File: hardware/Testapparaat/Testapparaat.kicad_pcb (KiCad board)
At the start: 2 copper layers, 138.9 x 89.6 mm, 107 parts, among them J1 IO_SD, J10 B-, J11 Display_shield, J12 GPIO_INPUTS, J13 FrontPanel, J14 GPIO_OUTPUT, J2 Module_1, J3 Module_2, J4 DEBUG, J5 FPC_40P_LCD_ILI9488, J6 IO_UART, J7 Emergency Stop Button, J8 CON-SOCJ-2155, J9 B+, Q1 BC817, Q2 BC817, Q3 BC817, Q4 IRFR9024N, Q5 IRFR9024N, Q6 IRFR9024N, SW1 RST, SW2 on/off switch, U1 74HC595 (SIPO Shift register), U10 LM2596S-5, U11 LM2596S-3.3, U12 74AUC1G74, U2 ESP32-WROOM-32, U4 74HC595 (SIPO Shift register), U5 TCA9534 (IO Expander), U6 74HC14, U7 TCA9534 (IO Expander), U8 74HC14, U9 74HC14

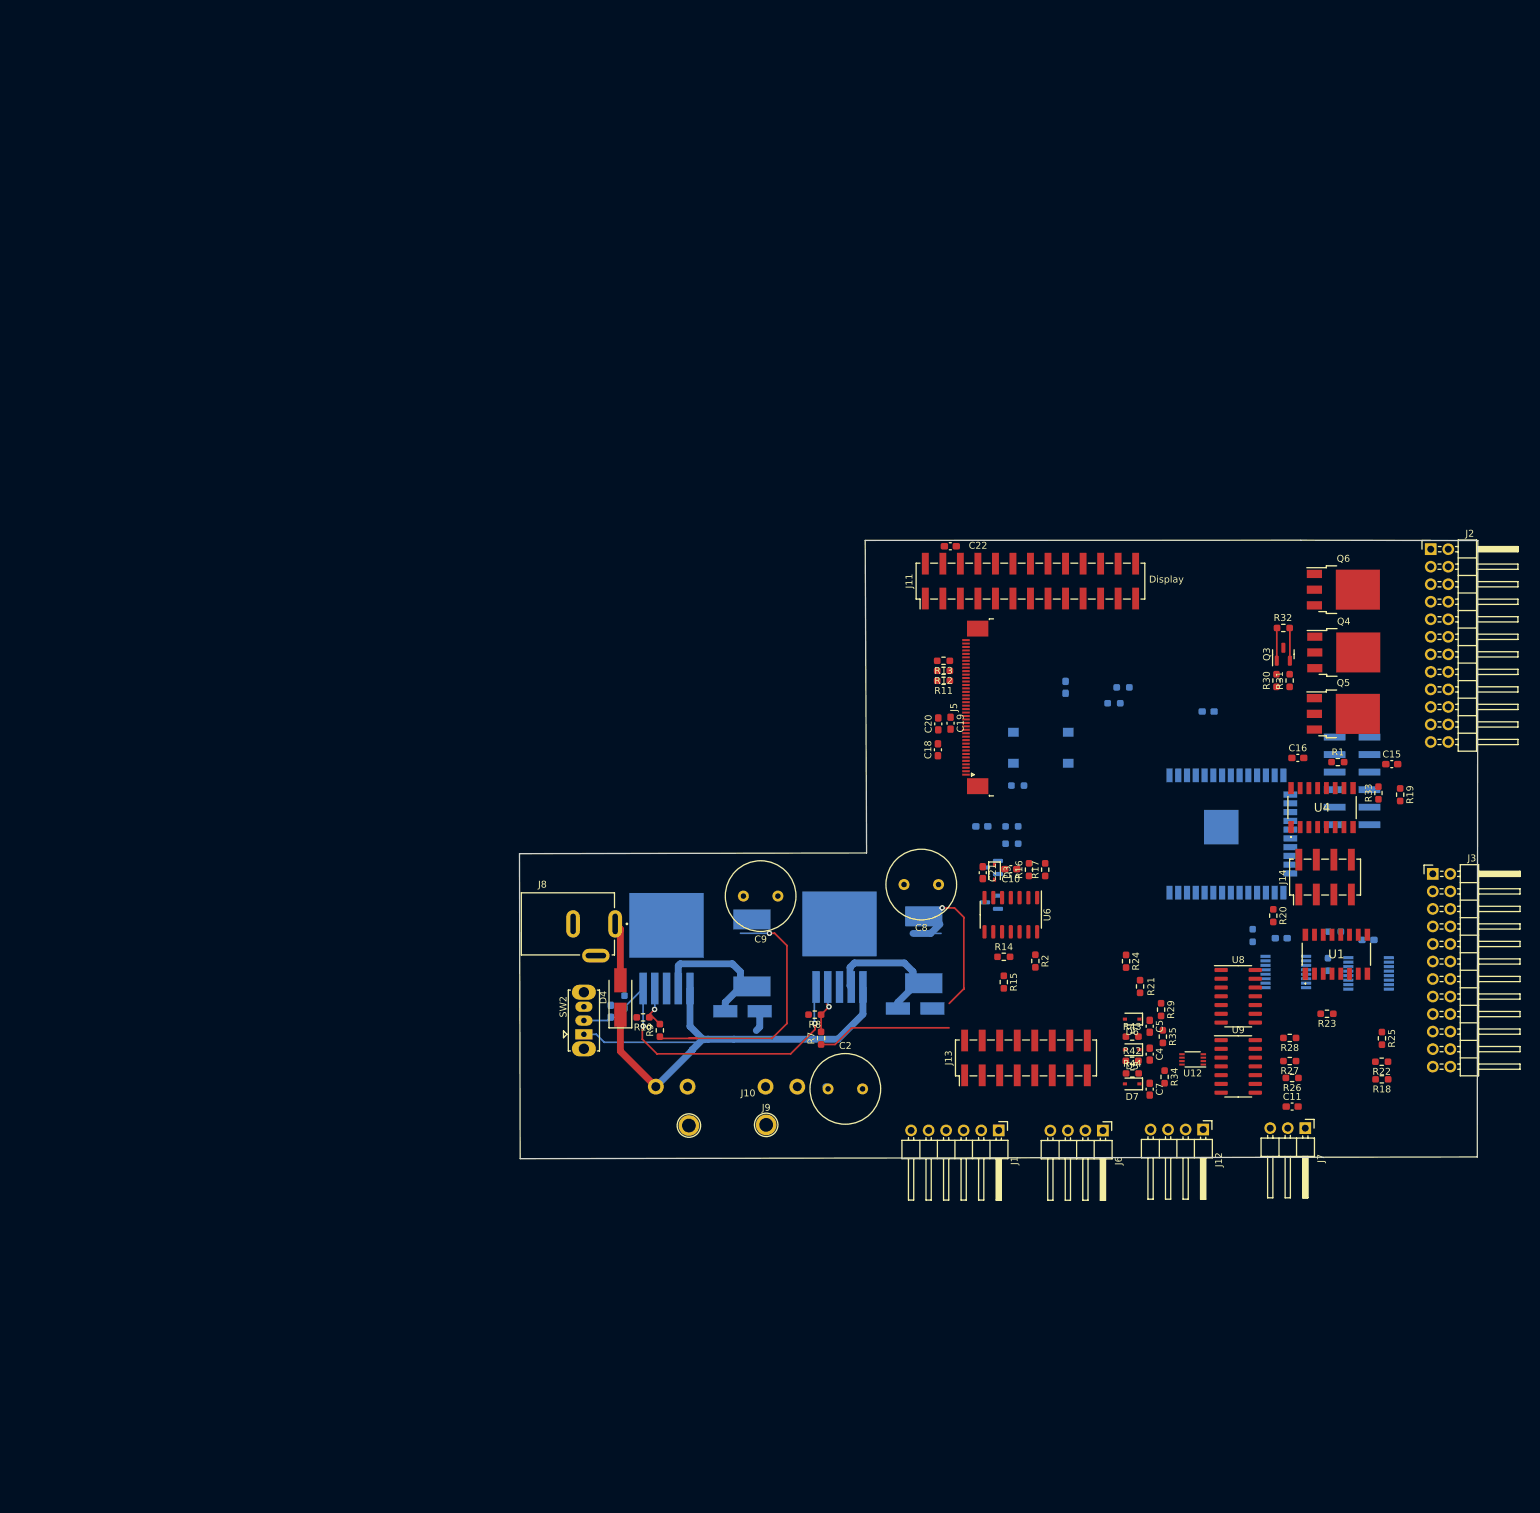
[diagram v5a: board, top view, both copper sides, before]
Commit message: -enh New pcb layout, may fit better in the existing case design
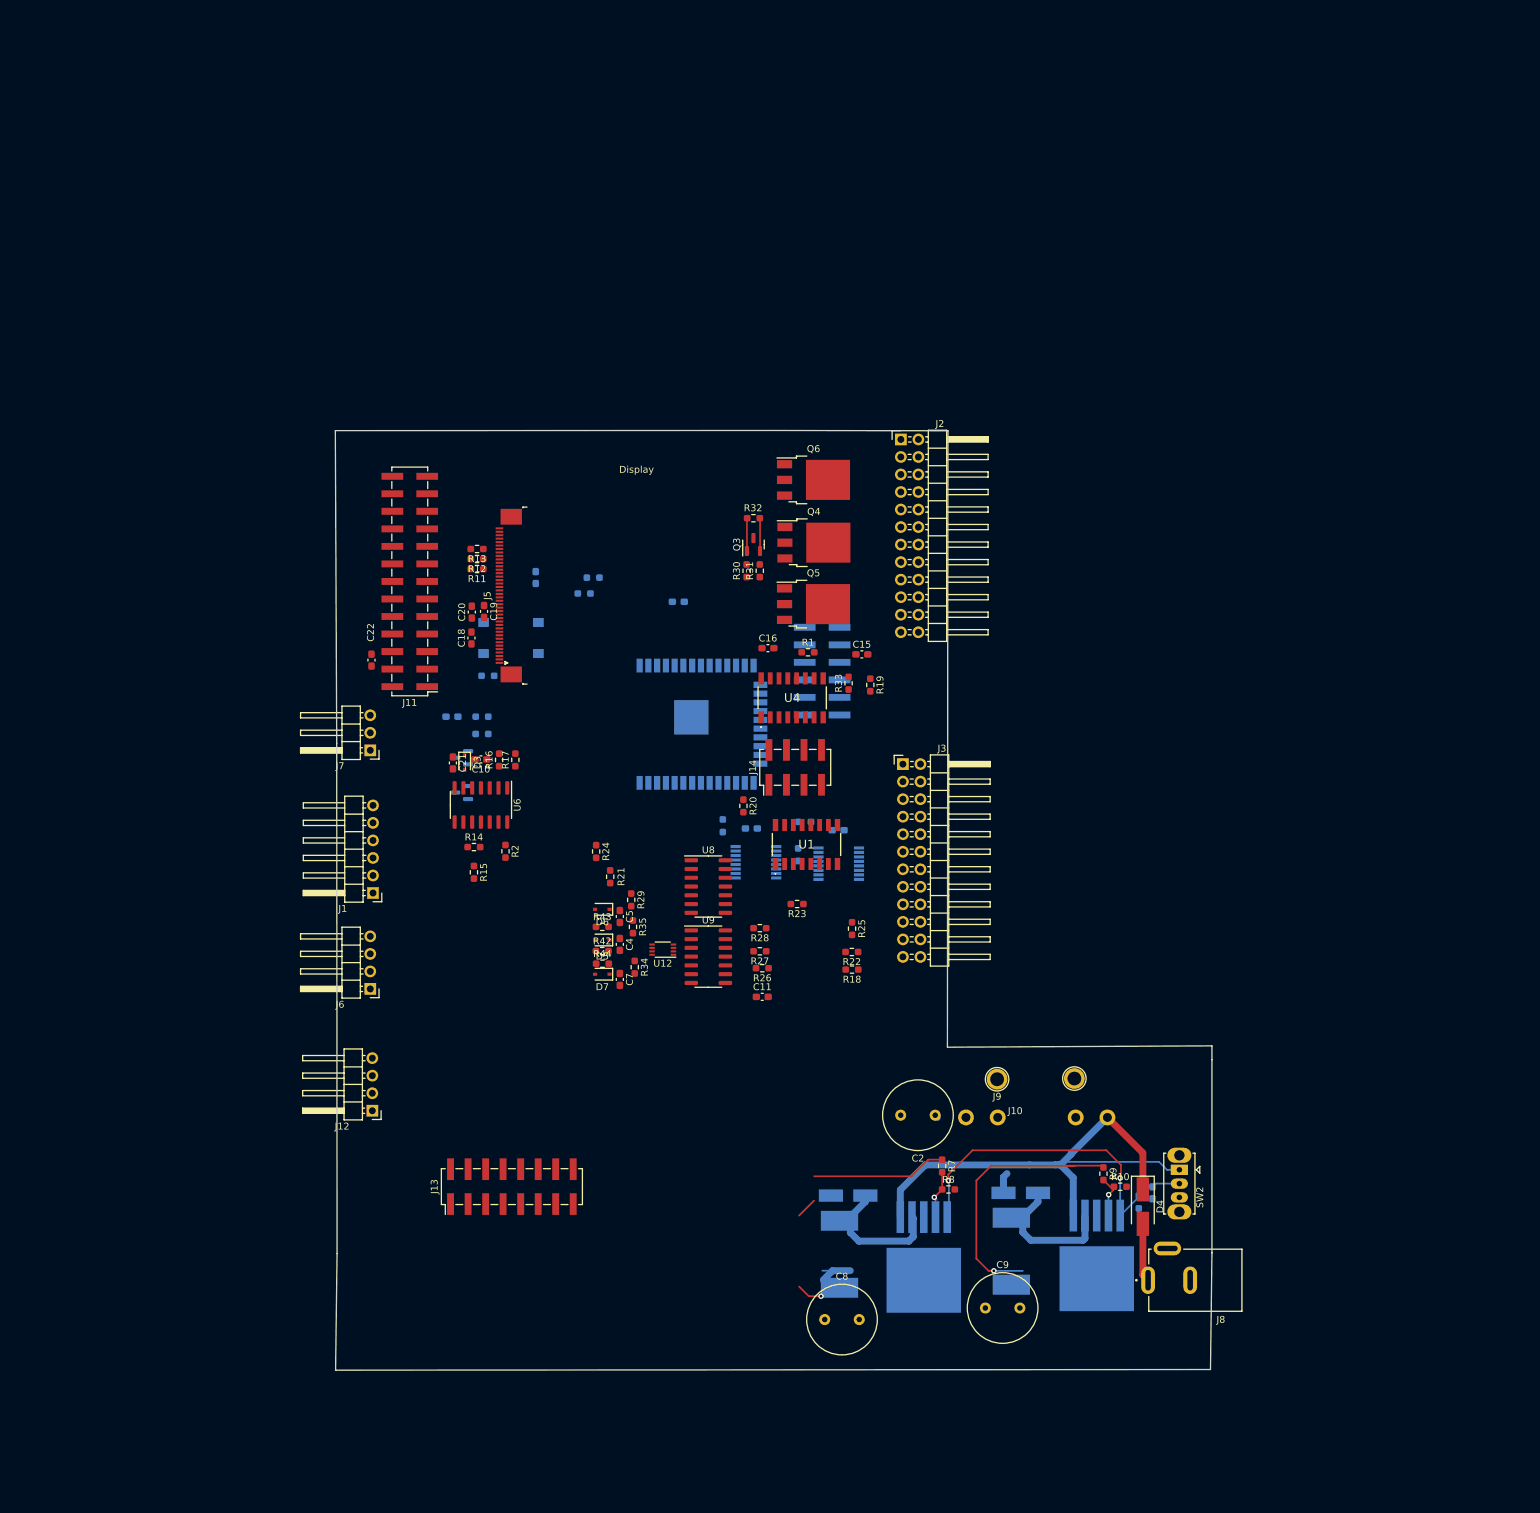
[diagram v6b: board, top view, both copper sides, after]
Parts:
- moved J7 146.1 mm to (99.8, 76.6), turned to 180 degrees
- moved J12 120.4 mm to (100.1, 128.9), turned to 180 degrees
- moved J6 108.1 mm to (99.8, 111.2), turned to 180 degrees
- moved J8 103.3 mm to (218.6, 153.4), turned to 180 degrees
- moved J1 97.0 mm to (100.2, 97.3), turned to 180 degrees
- moved J11 90.0 mm to (105.5, 52.2), turned to 180 degrees
- moved SW2 88.5 mm to (217.0, 137.4), turned to -90 degrees
- moved C22 85.5 mm to (99.9, 63.6), turned to 90 degrees
- moved C3 82.8 mm to (213.1, 140.8), turned to -90 degrees
- moved D4 81.5 mm to (211.7, 142.7), turned to -90 degrees
- moved R6 80.0 mm to (211.1, 142.1), turned to -90 degrees
- moved R4 78.4 mm to (116.0, 74.3)
- moved R5 78.4 mm to (116.0, 71.7)
- moved C10 78.4 mm to (115.8, 77.9)
- moved C11 78.4 mm to (156.6, 112.3)
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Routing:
- net +5V: track 45.4 -> 35.1 mm
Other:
- board size 138.9 x 89.6 mm -> 127 x 136.2 mm

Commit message: -enh pcb layout rev2
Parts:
- added REF**: MountingHole_3.2mm_M3_DIN965_Pad, MountingHole:MountingHole_3.2mm_M3_DIN965_Pad, F.Cu at (209.6, 162.4)
- added REF**: MountingHole_3.2mm_M3_DIN965_Pad, MountingHole:MountingHole_3.2mm_M3_DIN965_Pad, F.Cu at (99.1, 99.6)
- added REF**: MountingHole_3.2mm_M3_DIN965_Pad, MountingHole:MountingHole_3.2mm_M3_DIN965_Pad, F.Cu at (99.2, 161.2)
- added REF**: MountingHole_3.2mm_M3_DIN965_Pad, MountingHole:MountingHole_3.2mm_M3_DIN965_Pad, F.Cu at (180.3, 162.4)
- added REF**: MountingHole_3.2mm_M3_DIN965_Pad, MountingHole:MountingHole_3.2mm_M3_DIN965_Pad, F.Cu at (169.3, 30.1)
- added REF**: MountingHole_3.2mm_M3_DIN965_Pad, MountingHole:MountingHole_3.2mm_M3_DIN965_Pad, F.Cu at (181.4, 124.4)
- added REF**: MountingHole_3.2mm_M3_DIN965_Pad, MountingHole:MountingHole_3.2mm_M3_DIN965_Pad, F.Cu at (99.4, 30.4)
- added REF**: MountingHole_3.2mm_M3_DIN965_Pad, MountingHole:MountingHole_3.2mm_M3_DIN965_Pad, F.Cu at (215.7, 124.4)
- moved J11 42.4 mm to (147.9, 50.2)
- moved J12 19.3 mm to (101.6, 148.1)
- moved J6 19.3 mm to (101.3, 130.4)
- moved C22 12.0 mm to (100.4, 51.6)
- moved J1 12.0 mm to (100.6, 85.3)
- moved J7 12.0 mm to (100.2, 64.6)
- moved C20 10.3 mm to (115.8, 46.4)
- moved C19 10.3 mm to (117.4, 46.3)
- moved C18 8.89 mm to (116.9, 51.8)
- moved R11 8.57 mm to (116.9, 42.0)
- moved R12 8.57 mm to (116.9, 40.5)
- moved R13 8.57 mm to (116.9, 39.1)
- moved C2 7.34 mm to (174.4, 130.6)
- moved J5 6.68 mm to (122.3, 48.0)
- moved J8 6.66 mm to (216.2, 147.2)
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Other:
- board size 127 x 136.2 mm -> 127 x 142.2 mm

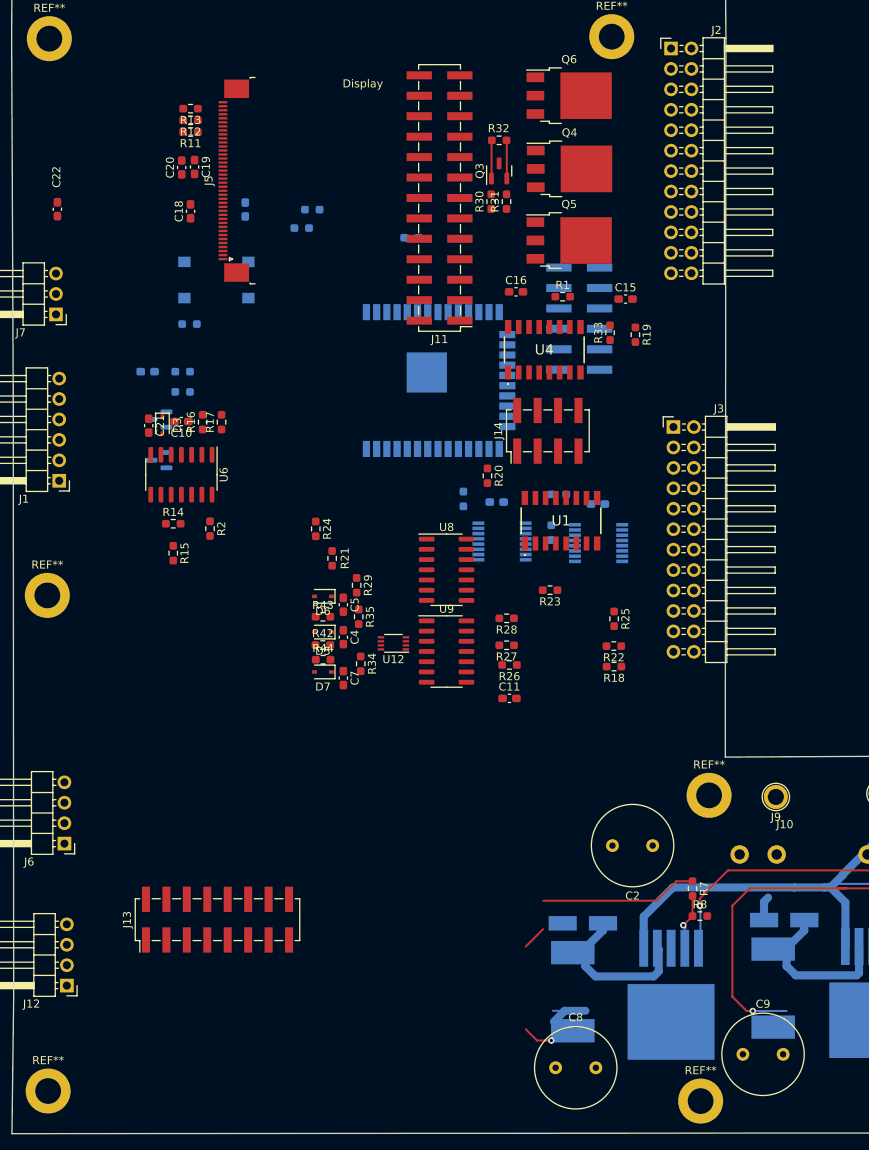
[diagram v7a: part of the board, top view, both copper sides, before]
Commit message: -enh component placing done:)
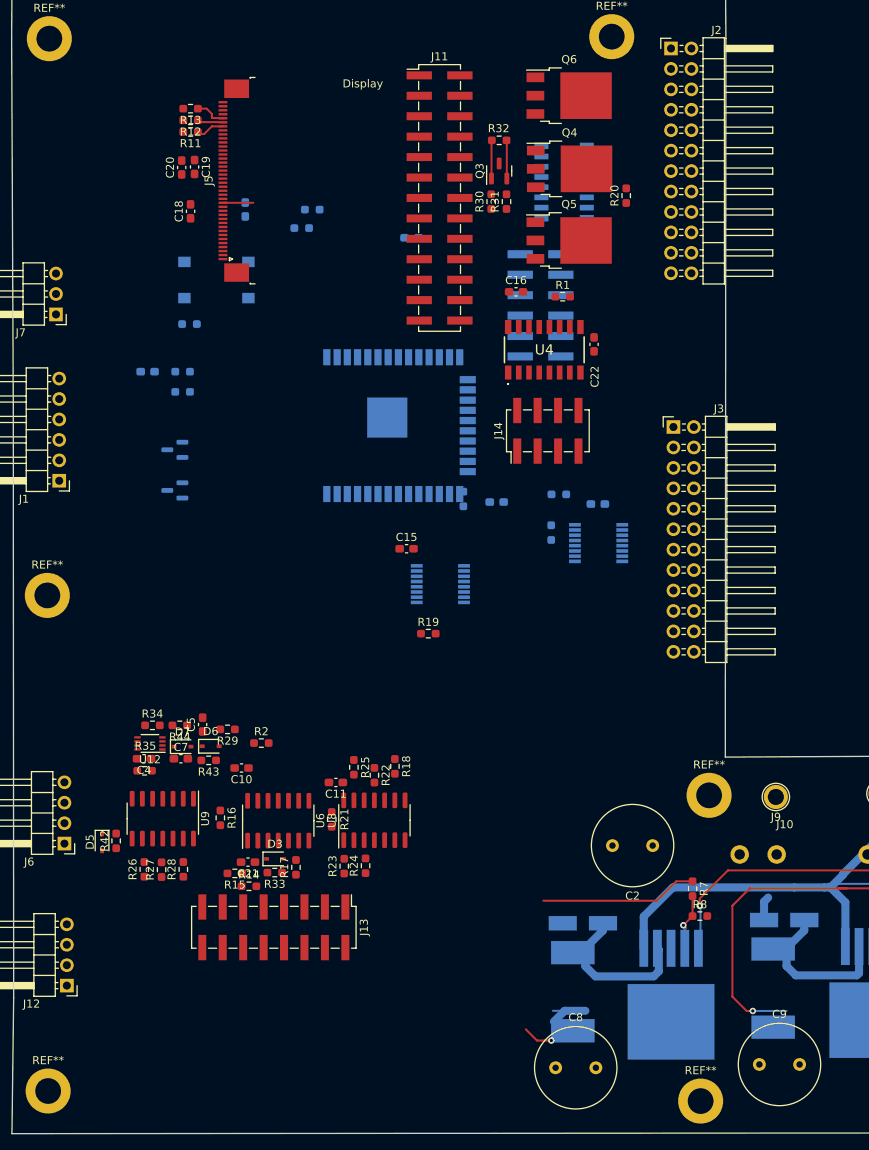
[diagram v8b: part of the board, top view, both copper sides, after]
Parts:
- U1: moved to B.Cu
- moved R33 79.0 mm to (127.4, 134.0), turned to 180 degrees
- moved C22 68.8 mm to (167.1, 68.4), turned to -90 degrees
- moved R17 56.1 mm to (130.0, 133.4)
- moved D3 55.7 mm to (127.4, 132.3), turned to 0 degrees
- moved C21 55.6 mm to (124.1, 132.7), turned to 180 degrees
- moved R26 52.0 mm to (111.2, 133.6), turned to 90 degrees
- moved R27 51.2 mm to (113.3, 133.6), turned to 90 degrees
- moved R28 50.9 mm to (116.0, 133.6), turned to 90 degrees
- moved R16 49.2 mm to (120.6, 127.2), turned to -90 degrees
- moved R14 46.0 mm to (124.2, 135.7)
- moved R19 45.2 mm to (146.5, 104.3), turned to 0 degrees
- moved U6 44.7 mm to (127.8, 127.6), turned to 90 degrees
- moved C10 43.7 mm to (123.3, 121.0)
- moved R23 42.8 mm to (136.0, 133.2), turned to 90 degrees
- moved R24 42.3 mm to (138.7, 133.2), turned to 90 degrees
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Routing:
- net Net-(J5-Pad36): track 0.00 -> 3.87 mm
- net Display_RST: track 0.00 -> 3.78 mm
- net Net-(J5-Pad34): track 0.00 -> 3.61 mm
- net +5V: track 35.1 -> 32.0 mm
- net Net-(J5-Pad35): track 0.00 -> 2.63 mm
